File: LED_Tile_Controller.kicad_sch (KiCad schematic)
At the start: 49 parts, among them J1 AVX 009159008061816, J4 Conn_01x04, J5 USB_C_Receptacle_USB2.0, J6 Stemma/QT, J7 Conn_01x02, J8 Conn_01x07, J9 Conn_02x03_Odd_Even, SW1 SW_Push, SW2 SW_Push, U2 ESP32-C3-MINI-1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

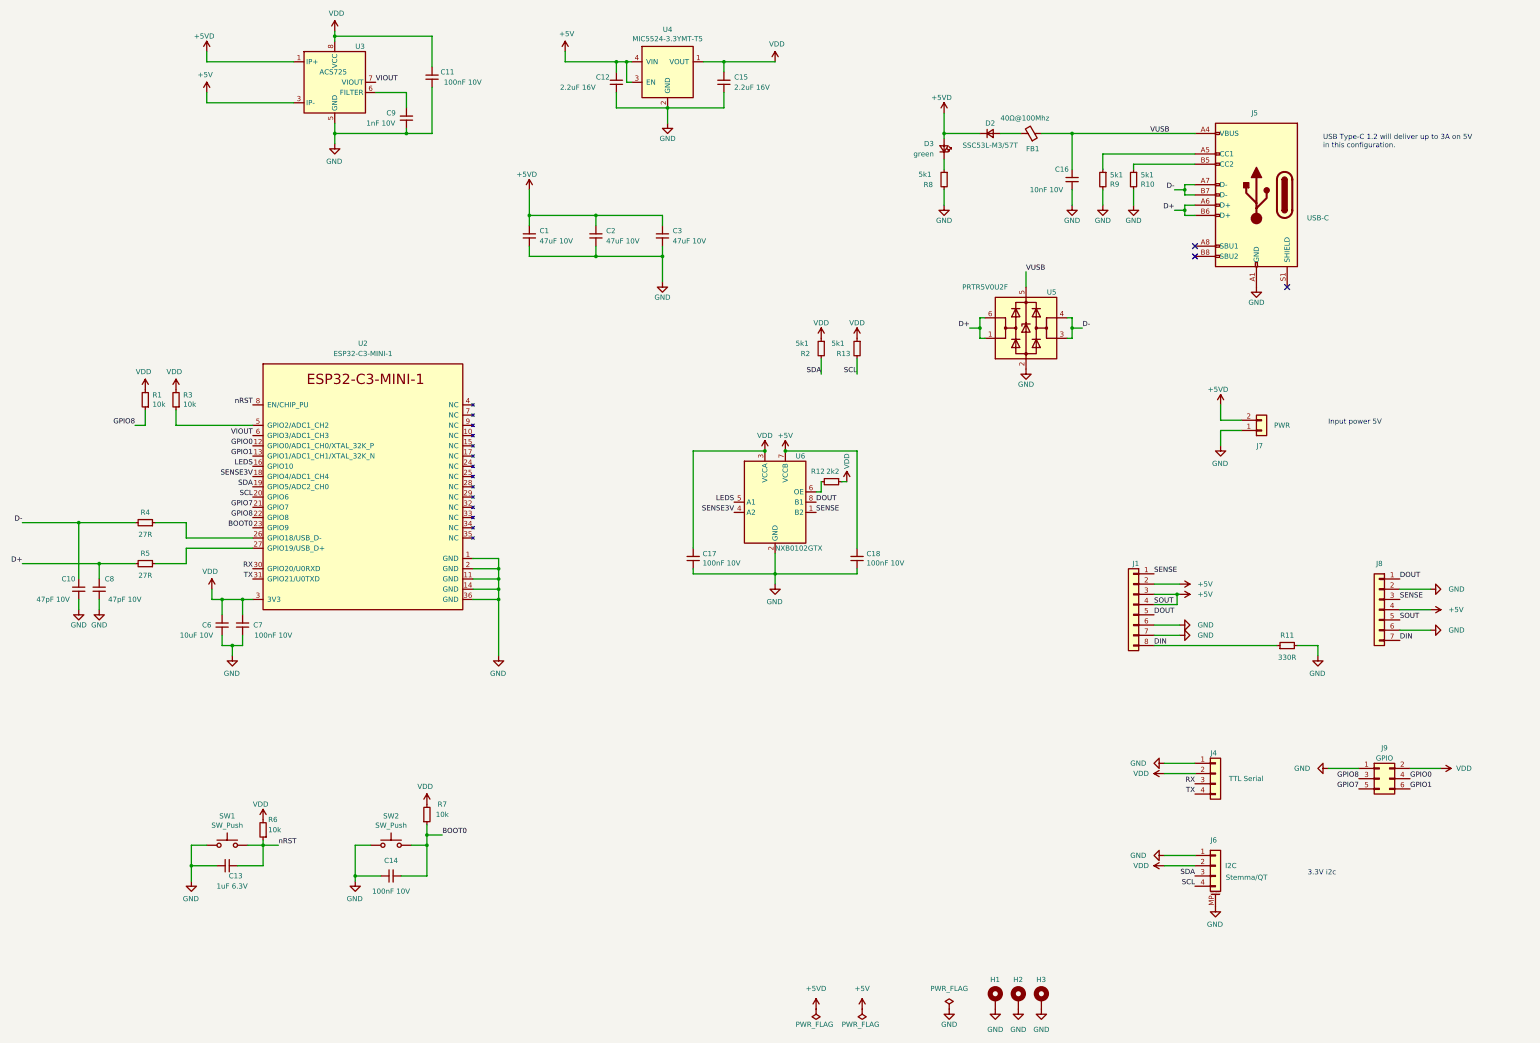
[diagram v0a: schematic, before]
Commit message: led tile controller working nicely :-)
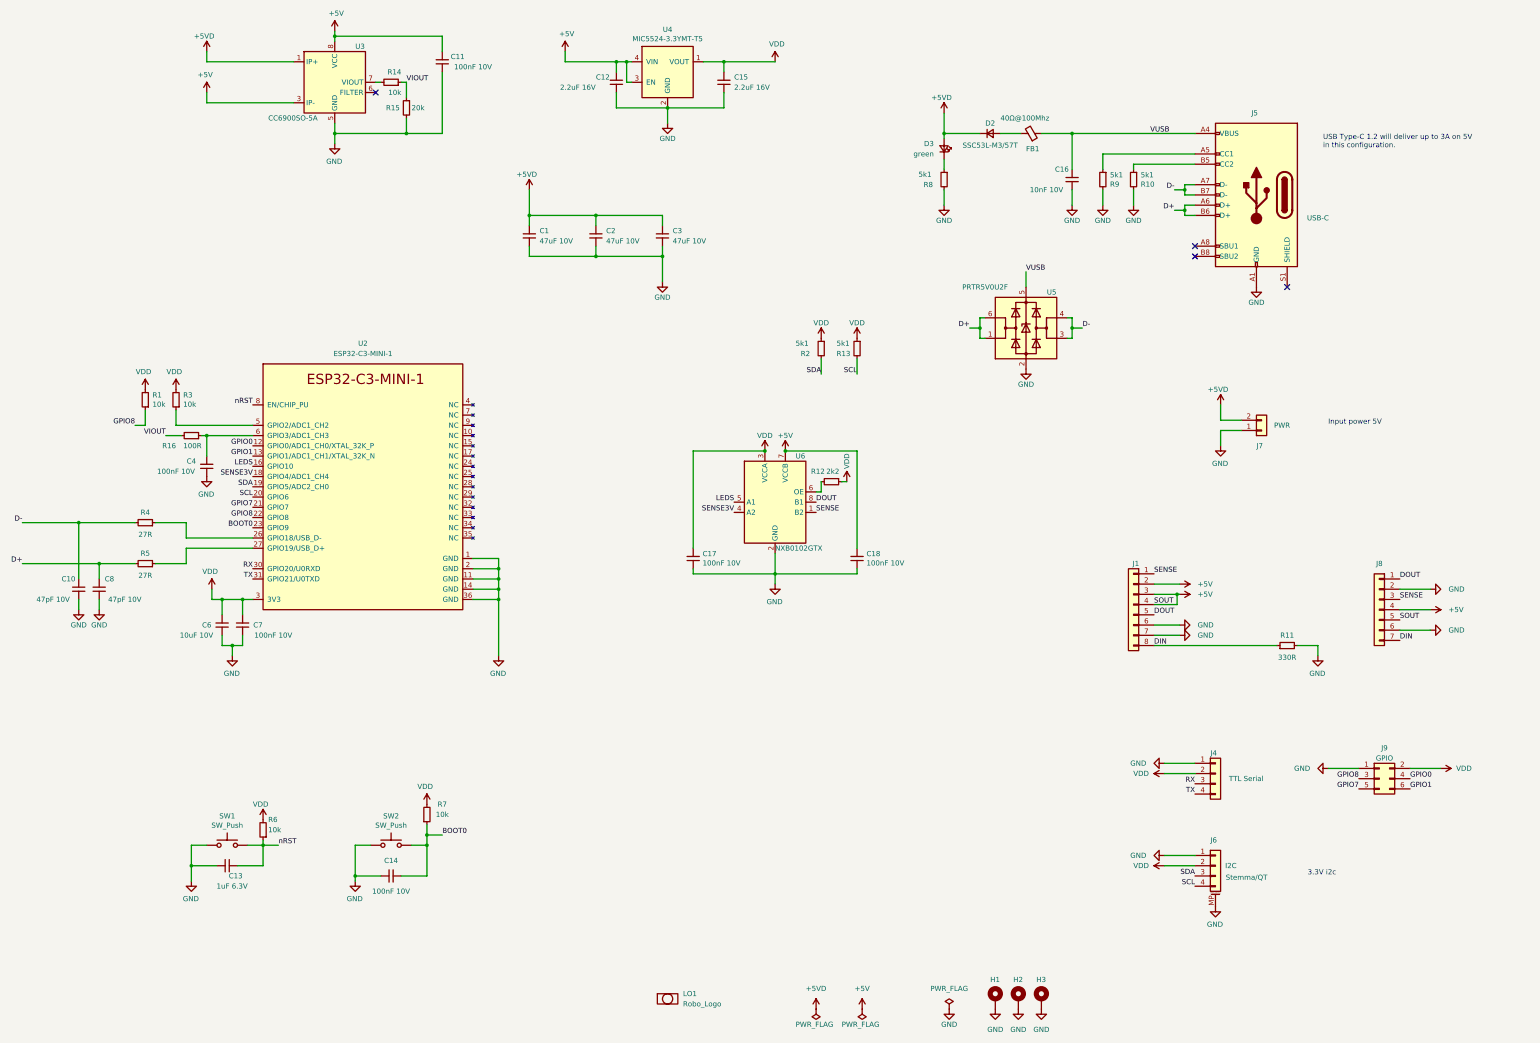
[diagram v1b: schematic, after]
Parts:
- removed C9: 1nF 10V, Capacitor_SMD:C_0402_1005Metric, symbol Device:C_Small
- added C4: 100nF 10V, Capacitor_SMD:C_0402_1005Metric, symbol Device:C_Small
- added LO1: Robo_Logo, runger:Robo_logo2, symbol runger:Robo_Logo
- added R14: 10k, Resistor_SMD:R_0402_1005Metric, symbol Device:R_Small
- added R15: 20k, Resistor_SMD:R_0402_1005Metric, symbol Device:R_Small
- added R16: 100R, Resistor_SMD:R_0402_1005Metric, symbol Device:R_Small
- H1, H2, H3, J7: now left out of the parts list
- R13, R2: Part Generic 1% -> Generic
- U3: value ACS725 -> CC6900SO-5A; Manu Allegro Microsystems -> Crosschip; Part ACS725LLCTR-10AB-T -> CC6900SO-5A
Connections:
- net +5V: now also C11.2, U3.8 (VCC)
- net GND: now also C4.1, R15.2
- net VDD: no longer C11.2, U3.8 (VCC)
- net VIOUT: now also R14.1, R15.1, R16.2; no longer U2.6 (GPIO3/ADC1_CH3), U3.7 (VIOUT)
- new net: R14.2, U3.7 (VIOUT)
- new net: C4.2, R16.1, U2.6 (GPIO3/ADC1_CH3)
- no-connect marks 3 -> 4
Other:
- moved on the sheet: C11
